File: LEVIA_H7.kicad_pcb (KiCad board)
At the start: 6 copper layers, 39.5 x 39.5 mm, 170 parts, among them J1 TF-028-H265, Q1 AO3400A, SW2 RKCGG140SMTRLFS, U1 USBLC6-2P6, U10 ZX-SH1.0-4PWT, U11 ZX-SH1.0-3PWT, U12 SIT1051TK/3, U13 ZX-SH1.0-4PWT, U14 ICM-42688-P, U15 ICM-42688-P, U16 DPS368XTSA1, U17 IST8310, U18 ZX-SH1.0-4PWT, U19 ZX-SH1.0-6PWT, U2 STM32H743VIHx, U20 ZX-SH1.0-6PWT, U21 ZX-SH1.0-3PWT, U22 ZX-SH1.0-8PWT, U24 ZX-SH1.0-4PWT, U3 ZX-SH1.0-4PWT, U4 LMR43620R5RPER, U5 LMR604303SRAKRQ1, U6 AP7361C-33FGE-7, U7 AP7361C-33FGE-7, U8 ZX-SH1.0-4PWT, U9 AT7456ELAH, Y1 8MHz, Y2 XL7EL89COI-111YLC-27M

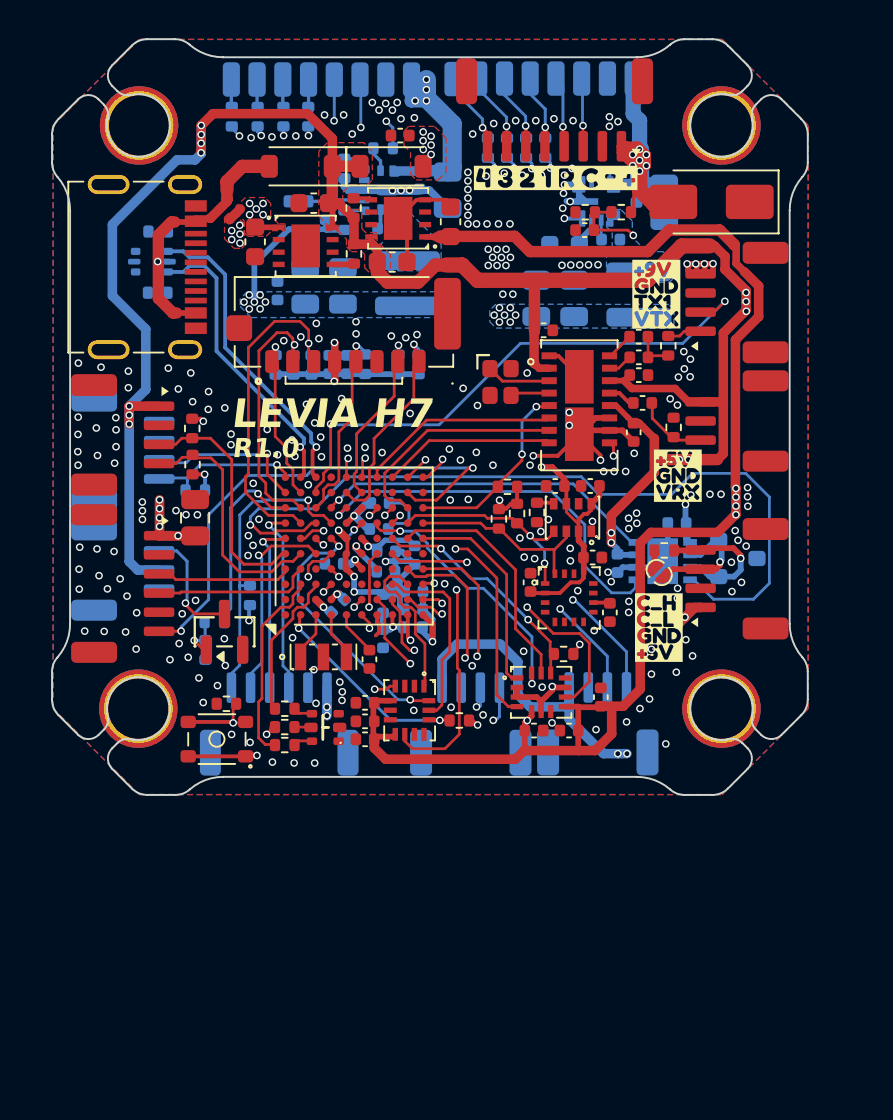
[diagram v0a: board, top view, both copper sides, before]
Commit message: USB impedance fix
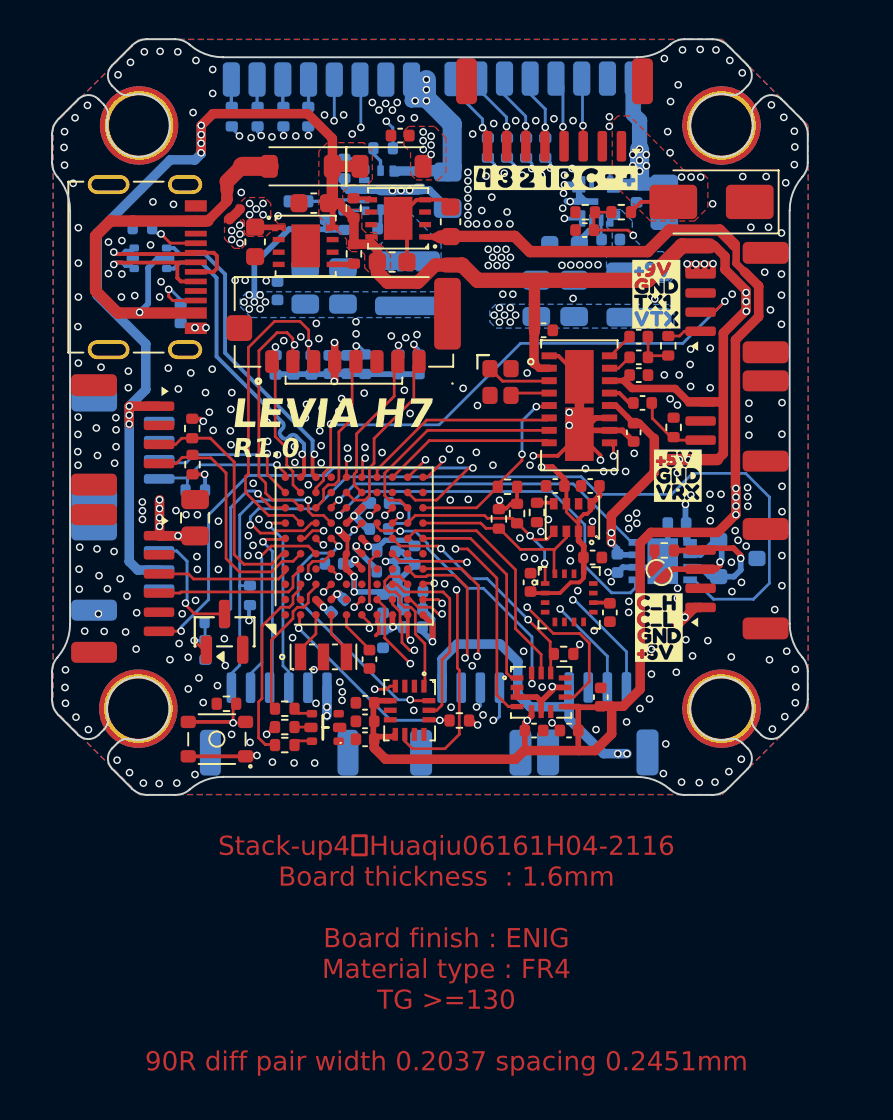
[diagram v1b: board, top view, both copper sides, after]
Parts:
- moved R2 1.61 mm to (125.7, 63.7), turned to -90 degrees
- moved R1 0.84 mm to (123.7, 59.2)
- moved U1 0.19 mm to (124.1, 60.8)
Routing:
- net VBAT: track 50.5 -> 25.1 mm, vias 11 -> 14
- net VBUS: track 14.1 -> 24.4 mm
- net /MCU/VDD: track 48.6 -> 38.3 mm
- net /USB_OTG.DN: track 0.00 -> 8.61 mm, vias 0 -> 1
- net /USB_OTG.DP: track 0.00 -> 7.43 mm, vias 0 -> 1
- net GND: track 63.2 -> 67.0 mm, vias 236 -> 364
- net Net-(USB1-CC2): track 0.00 -> 2.94 mm, vias 0 -> 1
- net Net-(USB1-CC1): track 0.00 -> 2.61 mm, vias 0 -> 1
- net +5V_SYS: track 185.7 -> 186.6 mm
- net /MCU/USB_OTG_P.DP: track 15.5 -> 16.3 mm
- net +9V: track 73.9 -> 74.6 mm
- added copper zone on F.Cu, net VBAT
- added copper zone on In2.Cu, net VBAT
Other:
- board text added: "Stack-up4：Huaqiu06161H04-2116 Board thickness : 1.6mm Board finish : ENIG Material type : FR4 TG >=130 90R diff pair width 0.2037 spacing 0.2451mm"
